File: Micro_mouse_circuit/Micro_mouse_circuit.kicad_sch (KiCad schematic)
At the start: 26 parts, among them J1 Conn_02x16_Odd_Even, J2 Battery input, J3 USB_C_Receptacle_PowerOnly_6P, J4 Conn_01x02, SW1 SW_SP3T, U1 LM2596SX-5_0/NOPB, U2 INA219AxDCN, U3 HUSB237-AA001-DN06R, U4 TP4056_C382139, U5 TYPE-C_6P_LTH6_5, U6 SN74LVC1G3157DCKR

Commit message: began schematic rev 3.0
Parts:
- removed D2: SS34_C8678, xxcustom_footprint:SMA_L4.3-W2.6-LS5.2-RD, symbol SS34_C8678:SS34_C8678
- removed D4: Green_LED, symbol Device:LED
- removed J2: Battery input, Connector_Wire:SolderWire-0.127sqmm_1x02_P3.7mm_D0.48mm_OD1mm, symbol Connector:Conn_01x02_Socket
- removed J3: USB_C_Receptacle_PowerOnly_6P, symbol Connector:USB_C_Receptacle_PowerOnly_6P
- removed J4: Conn_01x02, Connector_JST:JST_PH_S2B-PH-K_1x02_P2.00mm_Horizontal, symbol Connector_Generic:Conn_01x02
- removed R7: 0.1, symbol Device:R_Shunt
- removed R8: 2k, xxcustom_footprint:R0402, symbol Device:R_US
- removed R9: 6k, xxcustom_footprint:R0402, symbol Device:R_US
- removed SW1: SW_SP3T, symbol Switch:SW_SP3T
- removed U1: LM2596SX-5_0/NOPB, xxcustom_footprint:TO-263-5_L10.2-W8.9-P1.70-TL, symbol LM2596SX-5_0/NOPB:LM2596SX-5_0/NOPB
- removed U2: INA219AxDCN, Package_TO_SOT_SMD:SOT-23-8, symbol Sensor_Energy:INA219AxDCN
- removed U3: HUSB237-AA001-DN06R, xxcustom_footprint:TDFN-6_L2.0-W2.0-P0.65-TL-EP, symbol HUSB237-AA001-DN06R:HUSB237-AA001-DN06R
- removed U5: TYPE-C_6P_LTH6_5, xxcustom_footprint:USB-TYPE-C-SMD_TYPE-C-6P-LTH6.5, symbol TYPE-C_6P_LTH6_5:TYPE-C_6P_LTH6_5
- removed U6: SN74LVC1G3157DCKR, xxcustom_footprint:SC-70-6_L2.2-W1.3-P0.65-LS2.1-BR, symbol SN74LVC1G3157DCKR:SN74LVC1G3157DCKR
- added D1: SS34_C8678, xxcustom_footprint:SMA_L4.3-W2.6-LS5.2-RD, symbol SS34_C8678:SS34_C8678
- added D2: Green_LED, symbol Device:LED
- added J2: USB_C_Receptacle_PowerOnly_6P, symbol Connector:USB_C_Receptacle_PowerOnly_6P
- added J3: Conn_01x02, Connector_JST:JST_PH_S2B-PH-K_1x02_P2.00mm_Horizontal, symbol Connector_Generic:Conn_01x02
- added R1: 75k, symbol Device:R_US
- added R7: 6k, xxcustom_footprint:R0402, symbol Device:R_US
- added R8: 0.1, symbol Device:R_Shunt
- added U1: HUSB237-AA001-DN06R, xxcustom_footprint:TDFN-6_L2.0-W2.0-P0.65-TL-EP, symbol HUSB237-AA001-DN06R:HUSB237-AA001-DN06R
- added U2: SK22D15L5, xxcustom_footprint:SW-TH_XKB_SK22D15L7, symbol SK22D15L5:SK22D15L5
- added U3: LM2596SX-5_0/NOPB, xxcustom_footprint:TO-263-5_L10.2-W8.9-P1.70-TL, symbol LM2596SX-5_0/NOPB:LM2596SX-5_0/NOPB
- added U5: SN74LVC1G3157DCKR, xxcustom_footprint:SC-70-6_L2.2-W1.3-P0.65-LS2.1-BR, symbol SN74LVC1G3157DCKR:SN74LVC1G3157DCKR
- added U6: INA219AxDCN, Package_TO_SOT_SMD:SOT-23-8, symbol Sensor_Energy:INA219AxDCN
- C1: value 10uF -> 1uF
- C3: value C -> 10uF
- R3: value 1k -> 0.4; footprint xxcustom_footprint:R0402 -> (none)
- R5: value 0.4 -> 1k; footprint (none) -> xxcustom_footprint:R0402
- R6: value 75k -> 2k; footprint (none) -> xxcustom_footprint:R0402
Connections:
- net 5.5+: now also U5.5 (VCC)
- net 9V: now also C1.1, J2.A9 (VBUS), J2.B9 (VBUS), U1.2 (VUSB), U2.2, U3.1 (VIN); no longer C3.1
- net GND: now also J1.19 (Pin_19), J1.23 (Pin_23), D1.2 (A), J2.A12 (GND), J2.B12 (GND), J3.2 (Pin_2), R1.2, U1.7 (GND), U3.3 (GND), U3.5 (ON#/OFF), U3.6 (GND), U5.2 (GND), U6.3 (GND), U6.7 (A0); no longer R6.2
- net I2C1_SCL: now also U6.5 (SCL)
- net I2C1_SDA: now also U6.6 (SDA)
- net R_prog: now also R6.1, R7.1
- net at R4.1: now also U4.6 (STDBY#); no longer D3.1 (K)
- net at R4.2: now also D2.1 (K); no longer U4.7 (CHRG#)
- net at L1.1: now also D1.1 (K), U3.2 (OUTPUT)
- net at D3.2 (A): now also R3.2, D2.2 (A); no longer R5.2
- net 5V: now reaches R3.1
- net 5V: now also C2.1, L1.2, R2.1, U4.8 (CE), U3.4 (FB), U6.4 (VS), U6.8 (A1); no longer U4.6 (STDBY#)
- net Motor2_B_OUT: now reaches J1.1 (Pin_1)
- net MOTOR4_CTRL2: now reaches J1.10 (Pin_10)
- net EXT_LOAD2_OUT: now reaches J1.11 (Pin_11)
- net USART2_TX: now reaches J1.12 (Pin_12)
- net Battery: now reaches J1.14 (Pin_14)
- net Battery: now also C3.1, U4.5 (BAT), R8.4
- net 3V3 oUT: now reaches J1.18 (Pin_18)
- net Motor2_A_OUT: now reaches J1.2 (Pin_2)
- net 5V Out: now reaches J1.20 (Pin_20)
- net EXT_LOAD1_OUT: now reaches J1.21 (Pin_21)
- net MOTOR3_CTRL1: now reaches J1.24 (Pin_24)
- net CTRL_EXT_LOAD1: now reaches J1.25 (Pin_25)
- net MOTOR3_CTRL2: now reaches J1.26 (Pin_26)
- net MOTOR3_A_OUT: now reaches J1.27 (Pin_27)
- net MOTOR1_CTRL1: now reaches J1.28 (Pin_28)
- net MOTOR3_B_OUT: now reaches J1.29 (Pin_29)
- net Motor4_A_OUT: now reaches J1.3 (Pin_3)
- net MOTOR1_CTRL2: now reaches J1.30 (Pin_30)
- net MOTOR1_B_OUT: now reaches J1.31 (Pin_31)
- net MOTOR1_A_OUT: now reaches J1.32 (Pin_32)
- net MOTOR2_CTRL1: now reaches J1.4 (Pin_4)
- net Motor4_B_Out: now reaches J1.5 (Pin_5)
- net MOTOR2_CTRL2: now reaches J1.6 (Pin_6)
- net CTRL_EXT_LOAD2: now reaches J1.7 (Pin_7)
- net MOTOR4_CTRL1: now reaches J1.8 (Pin_8)
- net USART2_RX: now reaches J1.9 (Pin_9)
- removed net Buck_22: C2.1, L1.2, R2.1, R5.1, U4.8 (CE)
- removed net Charge+: C1.1, U4.5 (BAT)
- net fast_charge renamed FAST_CHARGE_CTRL
- net FAST_CHARGE_CTRL: now also U5.6 (S)
- new net: J3.1 (Pin_1), R8.1
- new net: R7.2, U5.3 (B1)
- new net: R6.2, U5.1 (B2)
- new net: R1.1, U1.3 (VSET)
- new net: J2.A5 (CC1), U1.1 (CC1)
- new net: J2.B5 (CC2), U1.6 (CC2)
- new net: R8.2, U6.1 (IN+)
- new net: R8.3, U6.2 (IN-)
- new net: R5.2, U4.7 (CHRG#)
- new net: D3.1 (K), R5.1
- new net 9V_in: U2.1
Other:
- note added: "Battery monitoring"
- note added: "Charging current selector"
- note added: "Switch"
- note added: "USB Recepticle and Power Delivery"
- note removed: "Battery monitor + switch"
- company: (none) -> University of Cape Town
- title: EEE3088_Micro_Mouse_Power_Sub_system -> EEE3088_Micro_Mouse_PCB

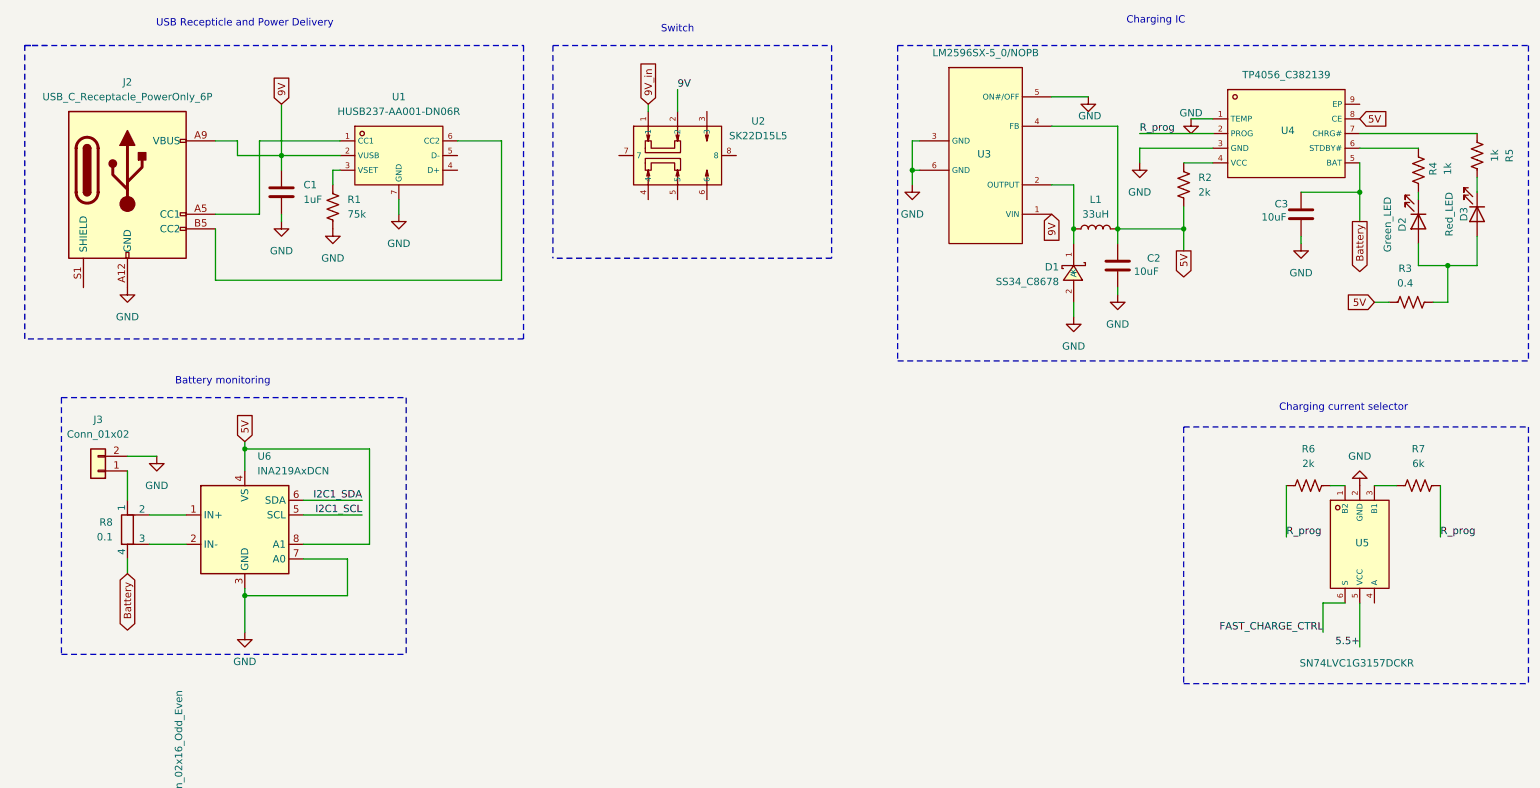
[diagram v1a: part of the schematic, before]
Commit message: adding footprint libraries
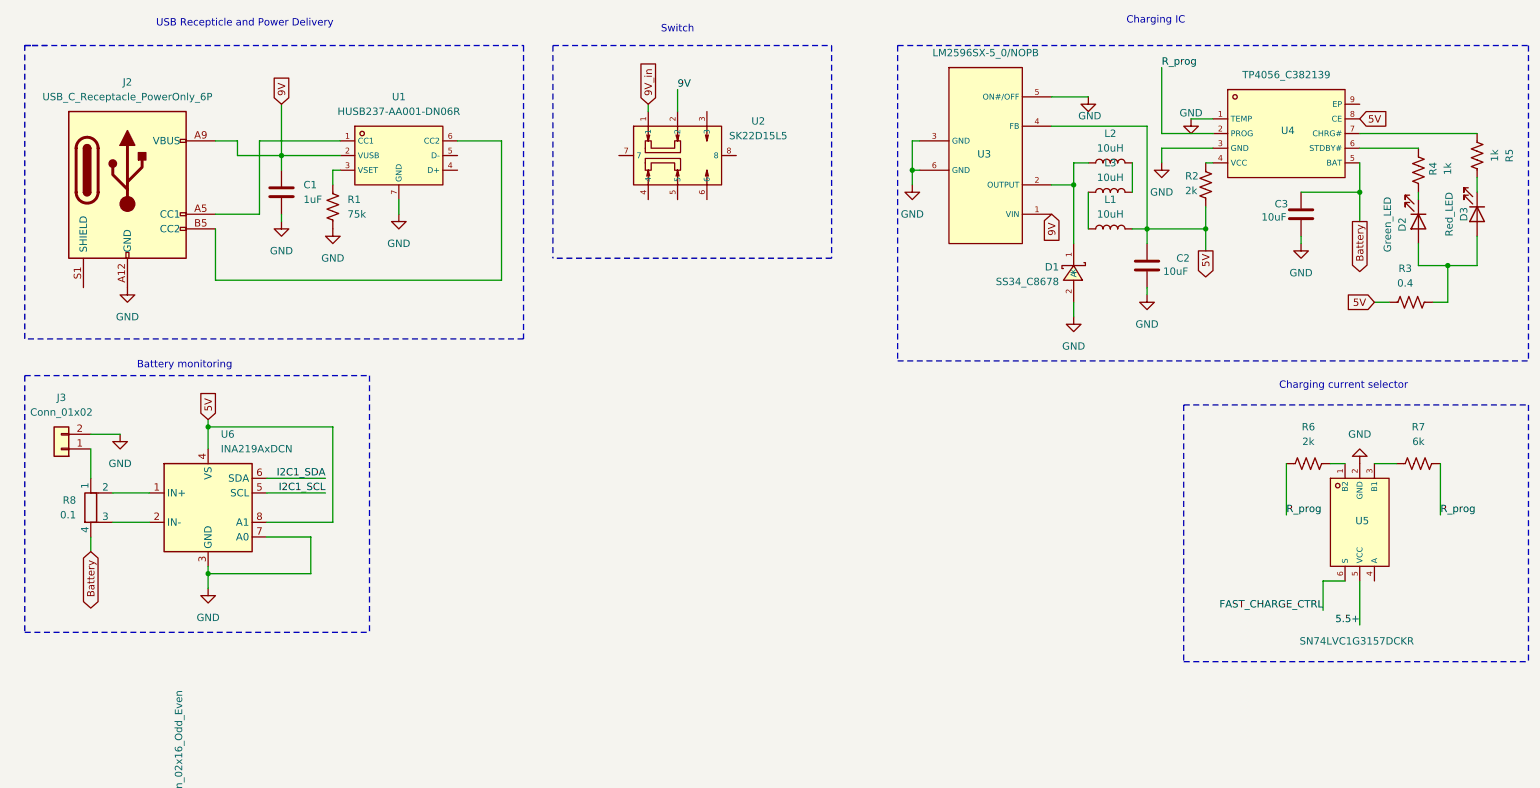
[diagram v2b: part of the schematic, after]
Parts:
- added L2, L3: 10uH, xxcustom_footprint:L0805, symbol Device:L
- L1: value 33uH -> 10uH; footprint (none) -> xxcustom_footprint:L0805
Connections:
- net at D1.1 (K), U3.2 (OUTPUT): now also L2.1; no longer L1.1
- new net: L1.1, L3.1
- new net: L2.2, L3.2
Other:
- moved on the sheet: C2, J3, L1, R2, R6, R7, R8, U5, U6

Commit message: assigned additional footprints
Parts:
- R8: value 0.1 -> 0.2A; footprint (none) -> xxcustom_footprint:R2512
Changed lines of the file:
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@@
 			)
 		)
-		(property "Value" "0.1"
+		(property "Value" "0.2A"
 			(at 24.13 101.5999 0)
 			(effects
@@
 			)
 		)
-		(property "Footprint" ""
+		(property "Footprint" "xxcustom_footprint:R2512"
 			(at 24.892 100.33 90)
 			(effects

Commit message: 4AM version of this circuit
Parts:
- added C4, C5, C6, C7, C9: C, symbol Device:C
- added C8: 680uF, symbol Device:C
- added D4: M7_C95872, footprint:SMA_L4.3-W2.6-LS5.2-RD, symbol M7_C95872:M7_C95872
- added D6: D_Schottky, symbol Device:D_Schottky
- added L4: L, symbol Device:L
- added R10, R11, R12, R13, R14, R15, R16, R9: R, symbol Device:R
- added U10: AMS1117-3.3, Package_TO_SOT_SMD:SOT-223-3_TabPin2, symbol Regulator_Linear:AMS1117-3.3
- added U11, U12: TPS22917DBV, Package_TO_SOT_SMD:SOT-23-6, symbol Power_Management:TPS22917DBV
- added U7: MT3608, Package_TO_SOT_SMD:SOT-23-6, symbol Regulator_Switching:MT3608
- added U8, U9: L298N_C19922, footprint:MULTIWATT-15_L19.6-W5.0-P1.27-L, symbol L298N_C19922:L298N_C19922
- C2: value 10uF -> 220uF
- R2: value 2k -> 0.4
- R8: value 0.2A -> 0.2
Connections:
- net 5.5+ is gone; now on net 5V: U5.5 (VCC)
- net 9V_in is gone; now on net 9V: U2.1
- net 5V: now also L3.2; no longer L1.2
- net 9V: no longer U2.2, U3.1 (VIN)
- net Battery: no longer C3.1, R8.4, U4.5 (BAT)
- net CTRL_EXT_LOAD1: now also U11.1 (VIN)
- net CTRL_EXT_LOAD2: now also U12.1 (VIN)
- net EXT_LOAD1_OUT: now also U11.6 (VOUT)
- net EXT_LOAD2_OUT: now also U12.6 (VOUT)
- net GND: now also C4.2, C5.2, C6.2, C7.2, C8.2, C9.2, R10.2, R11.1, R12.1, R13.1, R14.1, R16.2, U11.2 (GND), U12.2 (GND), U7.2 (GND), U8.8 (GND), U9.8 (GND)
- net MOTOR1_A_OUT: now also U8.2 (OUT_1)
- net MOTOR1_B_OUT: now also U8.3 (OUT_2)
- net MOTOR1_CTRL1: now also U8.5 (Input_1)
- net MOTOR1_CTRL2: now also U8.7 (Input_2)
- net MOTOR2_CTRL1: now also U9.5 (Input_1)
- net MOTOR2_CTRL2: now also U9.7 (Input_2)
- net MOTOR3_A_OUT: now also U8.13 (Out3)
- net MOTOR3_B_OUT: now also U8.14 (Out4)
- net MOTOR3_CTRL1: now also U8.10 (Input_3)
- net MOTOR3_CTRL2: now also U8.12 (Input_4)
- net MOTOR4_CTRL1: now also U9.10 (Input_3)
- net MOTOR4_CTRL2: now also U9.12 (Input_4)
- net Motor2_A_OUT: now also U9.2 (OUT_1)
- net Motor2_B_OUT: now also U9.3 (OUT_2)
- net Motor4_A_OUT: now also U9.13 (Out3)
- net Motor4_B_Out: now also U9.14 (Out4)
- net at D1.1 (K), U3.2 (OUTPUT): now also L1.1; no longer L2.1
- net at L3.1: now also L2.1; no longer L1.1
- net BatteryPos: now reaches U2.5
- net BatteryPos: now also R8.4, D4.1 (K)
- net SwitchOn: now reaches U2.6
- net SwitchOn: now also C4.1, L4.1, U7.5 (IN)
- net at L2.2: now also L1.2; no longer L3.2
- new net: R13.2, U9.1 (Sense_A)
- new net: C9.1, U12.4 (CT)
- new net: C3.1, D4.2 (A), U4.5 (BAT)
- new net: R15.2, R16.1, U10.1 (GND)
- new net: C7.1, U11.4 (CT)
- new net: D6.2 (A), L4.2, U7.1 (SW)
- new net: R11.2, U8.1 (Sense_A)
- new net: R10.1, R9.2, U7.3 (FB)
- new net: R12.2, U8.15 (Sense_B)
- new net: R14.2, U9.15 (Sense_B)
- new net 5VBoosted: C5.1, D6.1 (K), R9.1, U8.4 (VS), U8.9 (VSS), U9.4 (VS), U9.9 (VSS)
- new net SwitchCommon: C8.1, U2.2, U3.1 (VIN)
- new net V3.3Reg: R15.1, U10.2 (VO)
- new net VBoost: C6.1, U10.3 (VI)
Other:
- note added: "1"
- note added: "3.3V regulator"
- note added: "5V Boosted"
- note added: "5V Regulator"
- note added: "Motor 1 - Motor 4"
- note added: "Need to find suitable configuration of capacitors"
- moved on the sheet: C3
